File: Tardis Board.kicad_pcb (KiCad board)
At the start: 2 copper layers, 97.8 x 66 mm, 21 parts, among them J1 Conn_01x03_Female, Q1 IRLB8721PBF, SW1 SW_DIP_x01, SW2 SW_DIP_x01, SW3 SW_DIP_x01, SW4 SW_DIP_x01, SW5 SW_DIP_x01, SW6 SW_DIP_x01, SW7 SW_DIP_x01

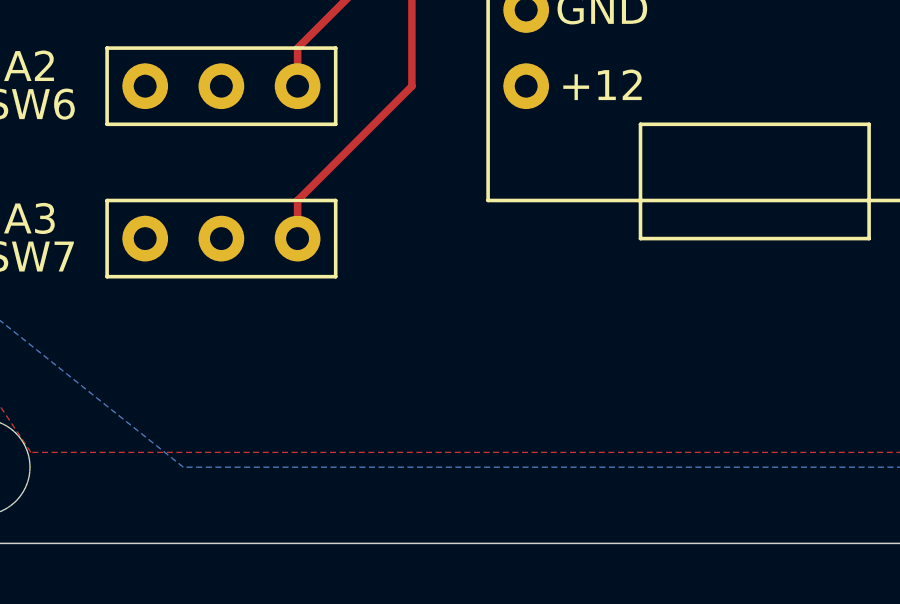
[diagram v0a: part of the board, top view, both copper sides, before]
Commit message: Added Sites for parts
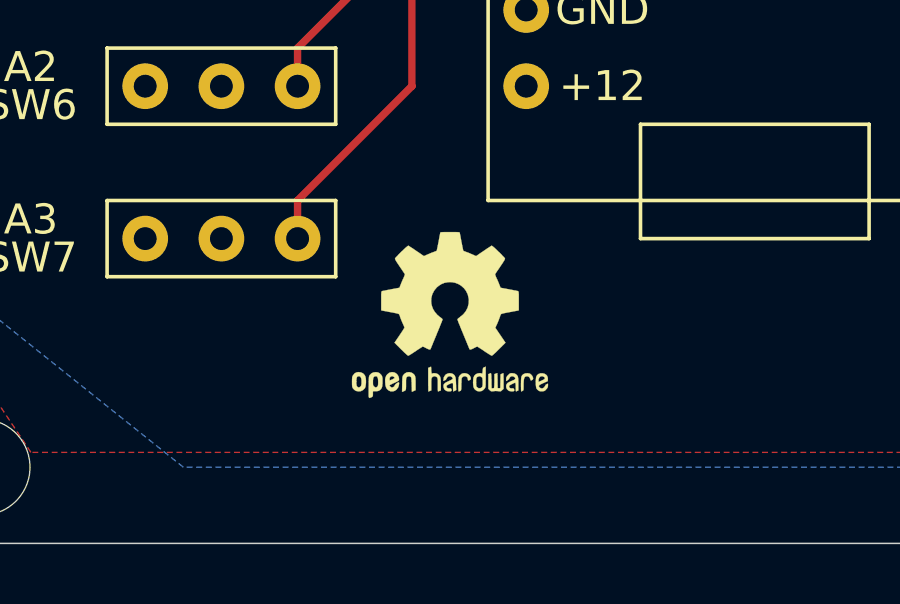
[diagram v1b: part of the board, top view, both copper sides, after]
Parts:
- added REF**: OSHW-Logo2_7.3x6mm_SilkScreen, Symbol:OSHW-Logo2_7.3x6mm_SilkScreen, F.Cu at (102.9, 99.1)
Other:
- board text added: "Amp: https://www.amazon.com/5V-12V-Amplifier-Module-Arduino-EK1236/dp/B01FDD3FYQ/ref=asc_df_B01FDD3FYQ/"
- board text added: "Arduino Pro Micro: https://www.sparkfun.com/products/12640"
- board text added: "Sound Board: https://www.adafruit.com/product/2341"
- board text added: "https://github.com/cmspooner/Sound-and-Light-Board"

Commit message: Version 2 Ordered
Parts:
- added D2: 1N5817, Diode_THT:D_DO-41_SOD81_P10.16mm_Horizontal, F.Cu at (127.0, 45.7)
- Q1: footprint Package_TO_SOT_THT:TO-220-3_Vertical -> Package_TO_SOT_THT:TO-220-3_Horizontal_TabDown
- SW2, SW3, SW4, SW5, SW6, SW7: value SW_DIP_x01 -> SW_SPDT
- moved REF** 69.8 mm to (172.7, 99.1)
- moved J1 19.7 mm to (143.5, 45.7)
- moved D1 19.5 mm to (108.0, 46.7), turned to 0 degrees
- moved NP1 17.2 mm to (108.0, 56.9)
- moved AMP2 17.1 mm to (158.1, 83.8)
- moved LS2 17.1 mm to (158.1, 91.4)
- moved AMP1 14.0 mm to (172.7, 83.8)
- moved LS1 14.0 mm to (172.7, 91.4)
- moved SW1 12.2 mm to (122.4, 48.3), turned to 90 degrees
- moved SW3 0.64 mm to (95.2, 75.6), turned to 0 degrees
- moved Q1 0.63 mm to (91.4, 64.1)
- turned SW2 to 0 degrees
- turned SW4 to 0 degrees
- turned SW5 to 0 degrees
- turned SW6 to 0 degrees
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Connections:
- Ard1 pad 21: /5_volt -> /5v
- J1 pad 1: /PowerSwitch -> Net-(D2-Pad2)
- NP1 pad 4: /5_volt -> /5v
- SFX1 pad 22: /5_volt -> /5v
- SW1 pad 2: /PowerSwitch -> Net-(D2-Pad1)
- SW2 pad 1: /SW14 -> /5v
- SW2 pad 2: GND -> /SW14
- SW2 pad 3: (no net) -> GND
- SW3 pad 1: /SW15 -> /5v
- SW3 pad 2: GND -> /SW15
- SW3 pad 3: (no net) -> GND
- SW4 pad 1: /SW18 -> /5v
- SW4 pad 2: GND -> /SW18
- SW4 pad 3: (no net) -> GND
- SW5 pad 1: /SW19 -> /5v
- SW5 pad 2: GND -> /SW19
- SW5 pad 3: (no net) -> GND
- SW6 pad 1: /SW20 -> /5v
- SW6 pad 2: GND -> /SW20
- SW6 pad 3: (no net) -> GND
- SW7 pad 1: /SW21 -> /5v
- SW7 pad 2: GND -> /SW21
- SW7 pad 3: (no net) -> GND
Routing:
- net /5v: track 0.00 -> 134.1 mm
- net /5_volt: track 94.6 -> 0.00 mm
- net Net-(AMP1-Pad2): track 38.8 -> 60.1 mm
- net Net-(D1-Pad1): track 7.62 -> 26.5 mm
- net Net-(Ard1-Pad14): track 23.7 -> 12.3 mm
- net /PowerSwitch: track 8.89 -> 0.00 mm
- net Net-(AMP2-Pad2): track 49.7 -> 42.9 mm
- net Net-(D2-Pad1): track 0.00 -> 4.57 mm
- net Net-(D2-Pad2): track 0.00 -> 3.81 mm
- net Net-(Ard1-Pad13): track 16.0 -> 17.1 mm
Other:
- board text added: "2x Amp: www.amazon.com/5V-12V-Amplifier-Module-Arduino-EK1236/dp/B01FDD3FYQ/"
- board text added: "A single amp can be used if mono sound is desired. If so, only attach the right amp and speaker."
- board text added: "All Auxillary Switches are attached to internal pull-up resistors in the Arduino."
- board text added: "Arduino Pro Micro: www.sparkfun.com/products/12640"
- board text added: "Main power is designed to use 12 volts DC, but anything 5 volts and above should work if usng lower powered LED Strip."
- board text added: "Schottky Diode 1N5817: www.mouser.com/ProductDetail/STMicroelectronics/1N5817/"
- board text added: "Sig"
- board text added: "Sound Board: www.adafruit.com/product/2341"
- board text removed: "Amp: https://www.amazon.com/5V-12V-Amplifier-Module-Arduino-EK1236/dp/B01FDD3FYQ/ref=asc_df_B01FDD3FYQ/"
- board text removed: "Arduino Pro Micro: https://www.sparkfun.com/products/12640"
- board text removed: "Sound Board: https://www.adafruit.com/product/2341"
